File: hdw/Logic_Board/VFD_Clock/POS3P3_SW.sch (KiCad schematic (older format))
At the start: 0 parts

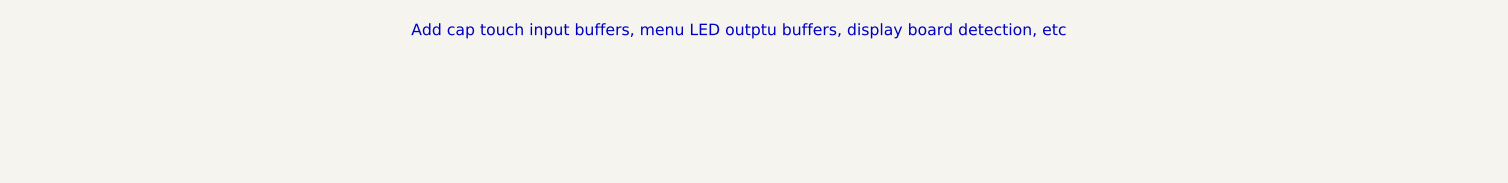
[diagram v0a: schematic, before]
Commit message: Added +3.3V SW sheet
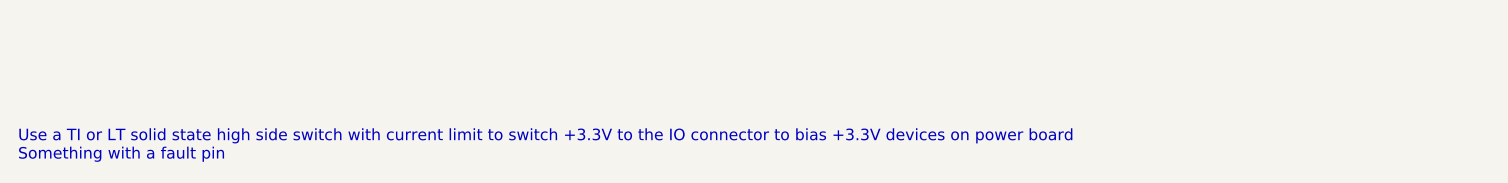
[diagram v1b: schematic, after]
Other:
- note added: "Use a TI or LT solid state high side switch with current limit to switch +3.3V to the IO connector to bias +3.3V devices on power board\nSomething with a fault pin"
- note removed: "Add cap touch input buffers, menu LED outptu buffers, display board detection, etc"
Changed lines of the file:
@@
 $Descr A 11000 8500
 encoding utf-8
-Sheet 21 22
+Sheet 22 22
 Title ""
 Date ""
@@
 Comment4 ""
 $EndDescr
-Text Notes 4410 3460 0    50   ~ 0
-Add cap touch input buffers, menu LED outptu buffers, display board detection, etc
+Text Notes 2690 4000 0    50   ~ 0
+Use a TI or LT solid state high side switch with current limit to switch +3.3V to the IO connector to bias +3.3V devices on power board\nSomething with a fault pin
 $EndSCHEMATC
